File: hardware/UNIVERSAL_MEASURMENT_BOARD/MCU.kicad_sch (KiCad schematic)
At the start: 14 parts, among them U1 STM32G484RET3, U2 ADS8863IDGS, Y1 ATX-H11-F-16.000MHz-G100-T

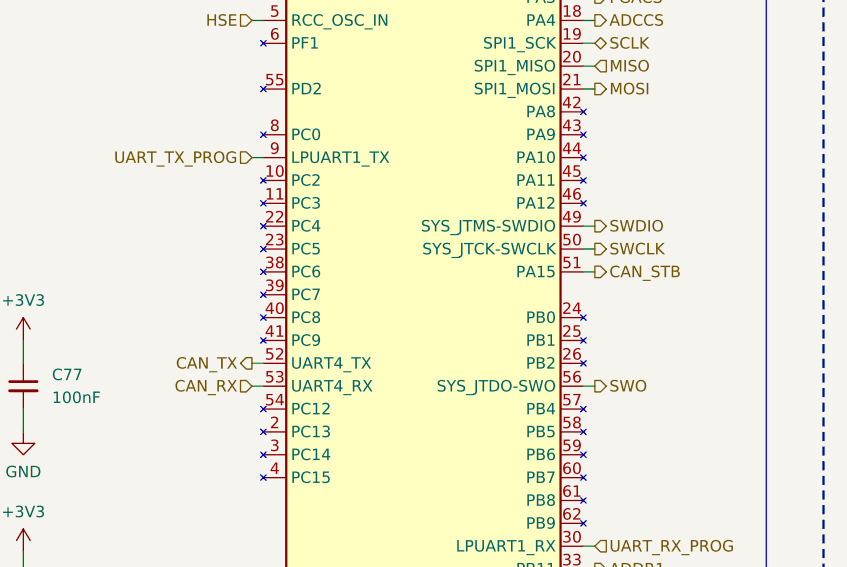
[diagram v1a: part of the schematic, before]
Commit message: Fixed VOUT range of PGA to 3.0V, fixed GPIO connection between FDCAN and MCU, added 1.5V VREF to PGA, changed value of enable divider of 7V DCDC converter.
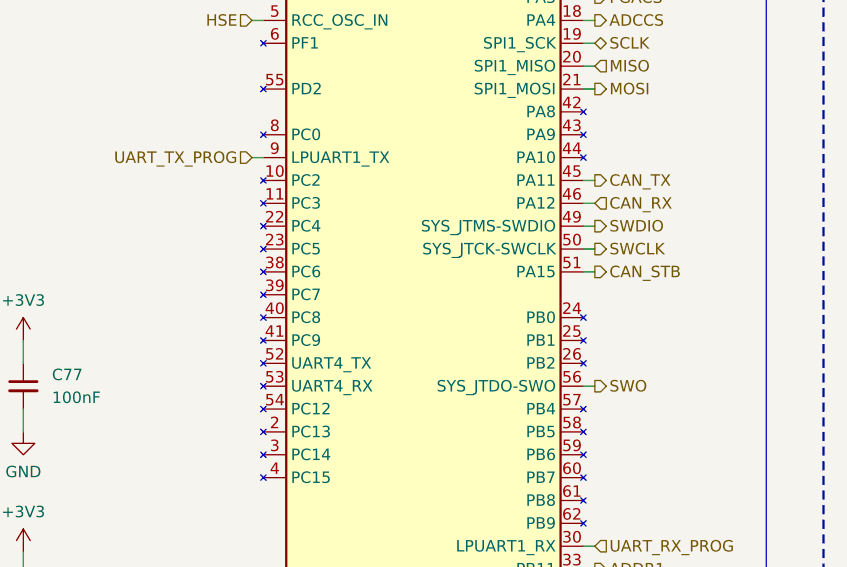
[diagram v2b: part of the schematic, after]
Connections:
- net CAN_RX: now also U1.46 (PA12); no longer U1.53 (PC11)
- net CAN_TX: now also U1.45 (PA11); no longer U1.52 (PC10)
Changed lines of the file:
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@@
 (kicad_sch
-	(version 20260101)
+	(version 20260306)
 	(generator "eeschema")
 	(generator_version "10.0")
@@
 		(title "Universal Measurment Board")
 		(date "2026-03-26")
-		(rev "1.9.21")
+		(rev "1.11.22")
 		(company "PUT Motorsport Formula Student Team")
 		(comment 1 "Designed by Marcin Trzmiel under")
@@
 	(wire
 		(pts
+			(xy 127 91.44) (xy 125.73 91.44)
+		)
+		(stroke
+			(width 0)
+			(type default)
+		)
+	)
+	(wire
+		(pts
 			(xy 107.95 51.435) (xy 107.95 53.34)
 		)
@@
 	(wire
 		(pts
+			(xy 127 88.9) (xy 125.73 88.9)
+		)
+		(stroke
+			(width 0)
+			(type default)
+		)
+	)
+	(wire
+		(pts
 			(xy 208.28 67.31) (xy 220.98 67.31)
 		)
@@
 	(wire
 		(pts
-			(xy 88.9 109.22) (xy 90.17 109.22)
-		)
-		(stroke
-			(width 0)
-			(type default)
-		)
-	)
-	(wire
-		(pts
 			(xy 208.28 66.04) (xy 208.28 67.31)
 		)
@@
 		(pts
 			(xy 127 96.52) (xy 125.73 96.52)
-		)
-		(stroke
-			(width 0)
-			(type default)
-		)
-	)
-	(wire
-		(pts
-			(xy 88.9 111.76) (xy 90.17 111.76)
 		)
 		(stroke
@@
 		)
 	)
+	(hierarchical_label "CAN_TX"
+		(shape output)
+		(at 127 88.9 0)
+		(effects
+			(font
+				(size 1.27 1.27)
+			)
+			(justify left)
+		)
+	)
 	(hierarchical_label "PGACS"
 		(shape output)
@@
 		)
 	)
-	(hierarchical_label "CAN_TX"
-		(shape output)
-		(at 88.9 109.22 180)
-		(effects
-			(font
-				(size 1.27 1.27)
-			)
-			(justify right)
-		)
-	)
 	(hierarchical_label "SWDIO"
 		(shape output)
@@
 	(hierarchical_label "CAN_RX"
 		(shape input)
-		(at 88.9 111.76 180)
-		(effects
-			(font
-				(size 1.27 1.27)
-			)
-			(justify right)
-		)
-	)
+		(at 127 91.44 0)
+		(effects
+			(font
+				(size 1.27 1.27)
+			)
+			(justify left)
+		)
+	)

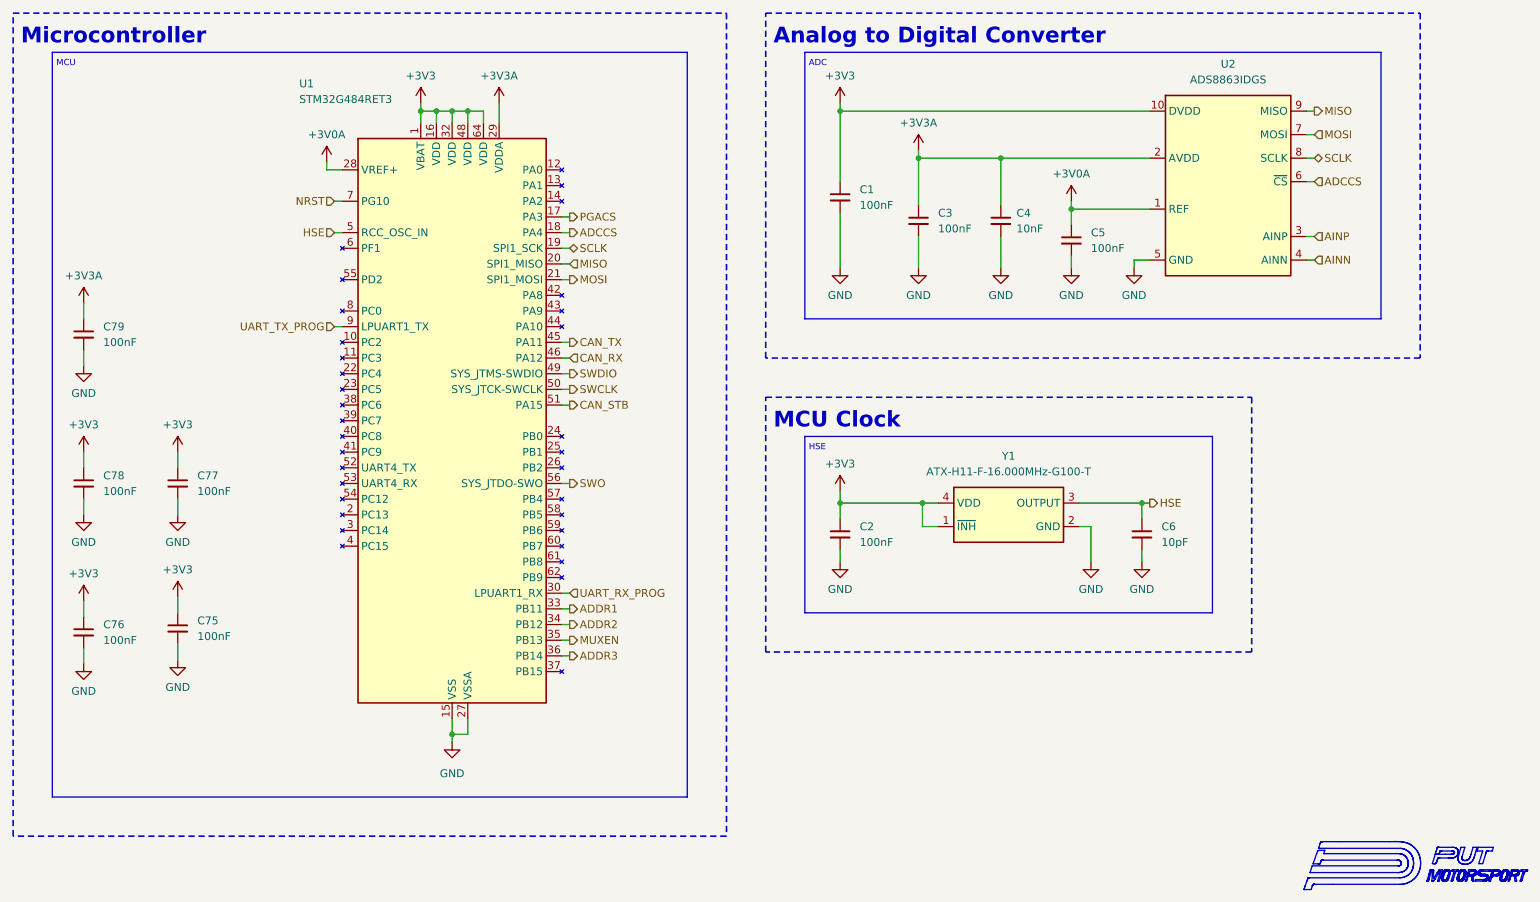
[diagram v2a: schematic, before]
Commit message: Reduced PCB dimensions, working on power section
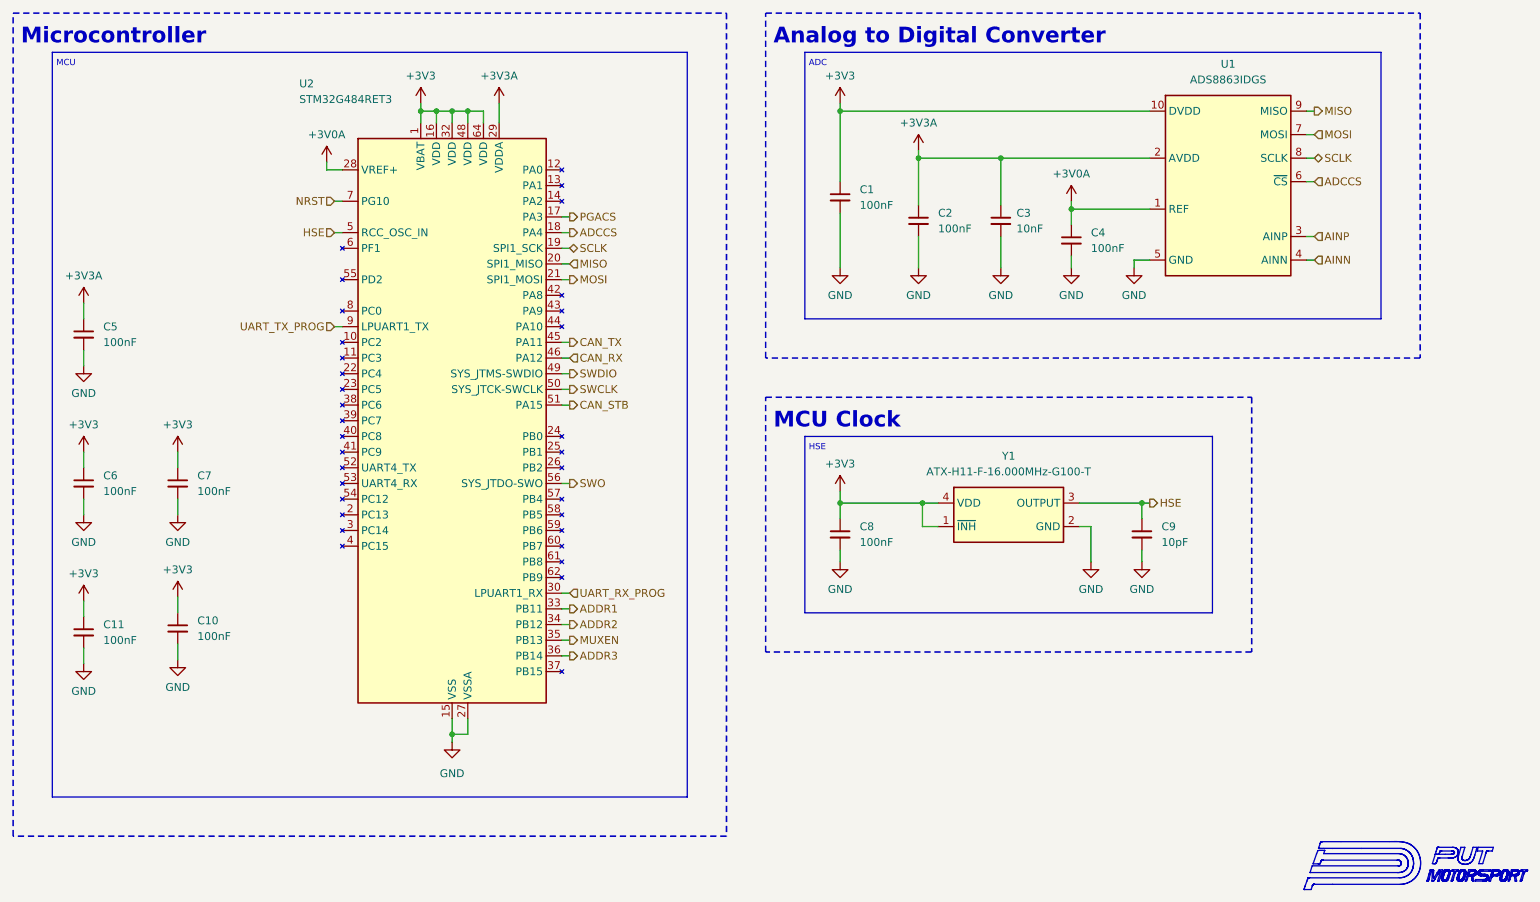
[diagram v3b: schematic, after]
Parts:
- renumbered C75 to C10, C76 to C11, C3 to C2, C4 to C3, C5 to C4, C79 to C5, C78 to C6, C77 to C7, C2 to C8, C6 to C9, U2 to U1, U1 to U2

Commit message: Finish PCB routing
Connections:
- net ADDR1: now also U2.43 (PA9); no longer U2.33 (PB11)
- net ADDR2: now also U2.44 (PA10); no longer U2.34 (PB12)
- net ADDR3: now also U2.45 (PA11); no longer U2.36 (PB14)
- net CAN_RX: now also U2.35 (PB13); no longer U2.46 (PA12)
- net CAN_STB: now also U2.33 (PB11); no longer U2.51 (PA15)
- net CAN_TX: now also U2.34 (PB12); no longer U2.45 (PA11)
- net MUXEN: now also U2.46 (PA12); no longer U2.35 (PB13)

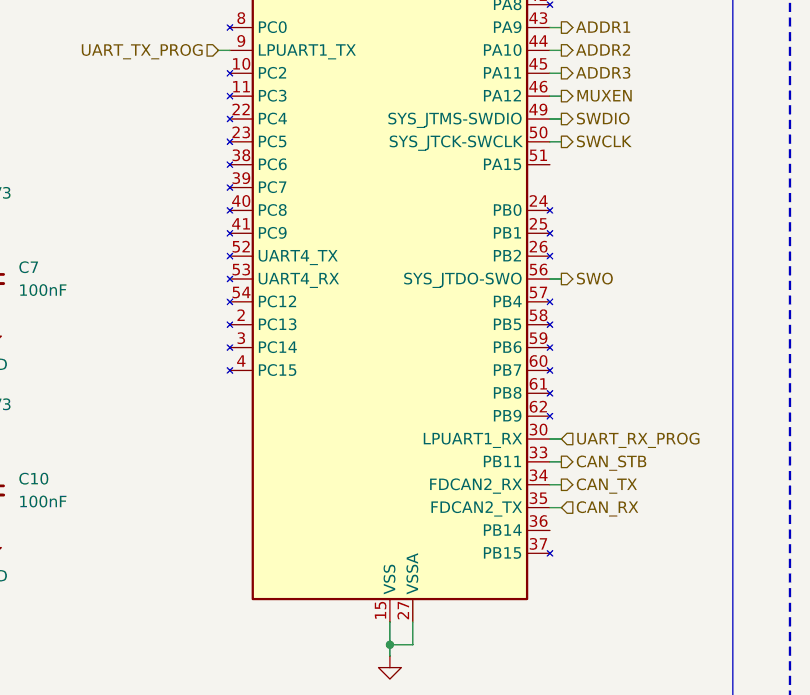
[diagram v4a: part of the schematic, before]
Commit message: Solved ERC & DRC
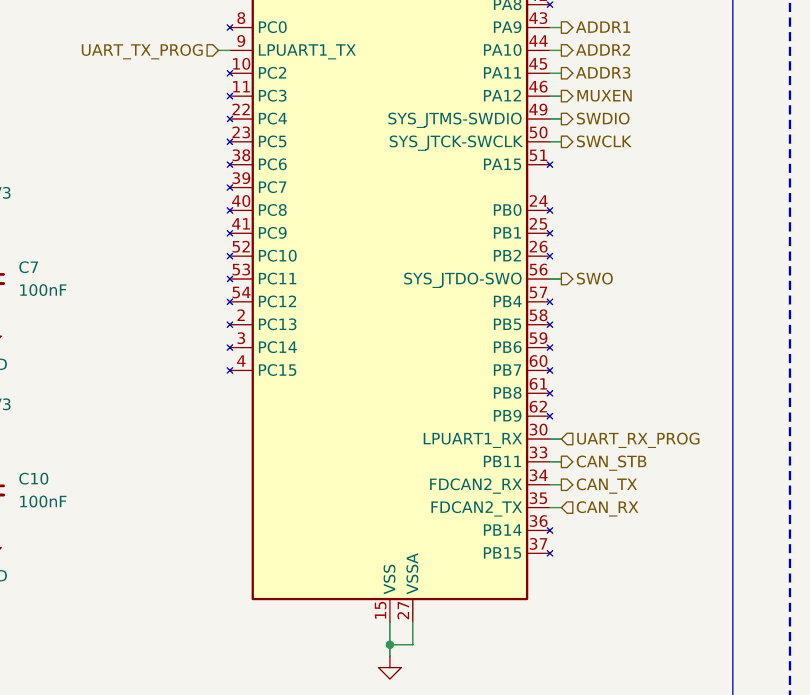
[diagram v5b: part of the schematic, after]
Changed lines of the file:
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@@
 		)
 		(pin "53"
-			(alternate "UART4_RX")
 		)
 		(pin "22"
@@
 		)
 		(pin "52"
-			(alternate "UART4_TX")
 		)
 		(pin "3"
